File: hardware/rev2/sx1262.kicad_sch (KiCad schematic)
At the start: 35 parts, among them U2 SX1262IMLTRT, U3 PE4259, Y2 TCXO 32MHz

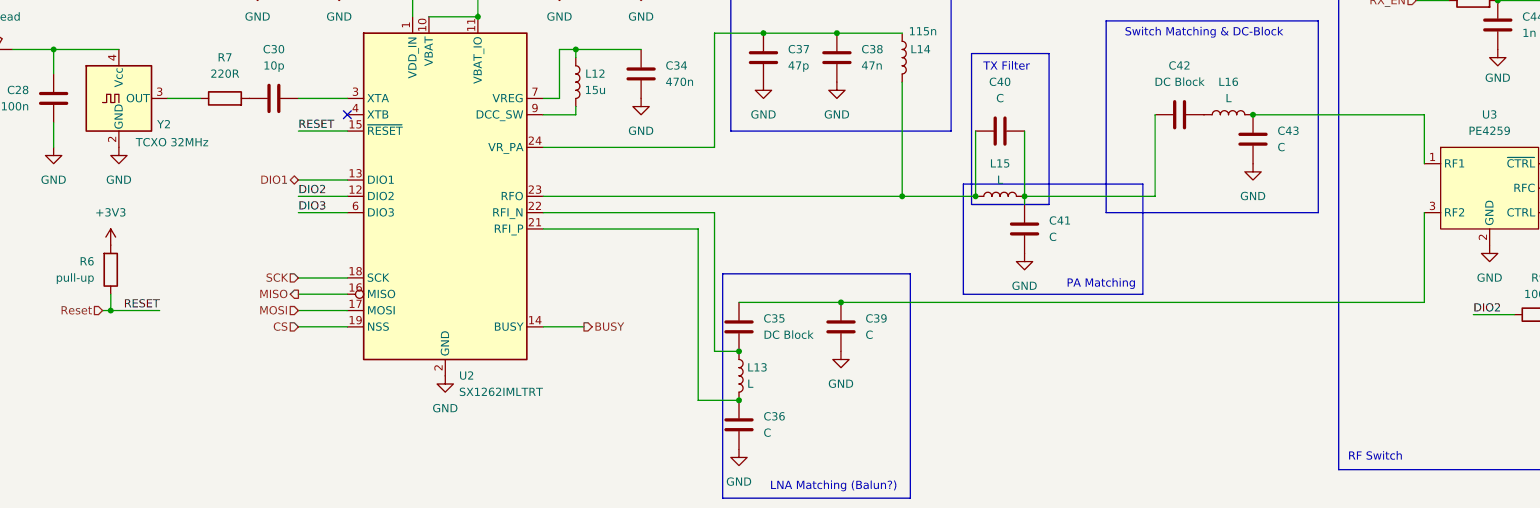
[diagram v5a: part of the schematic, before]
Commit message: fixed some ERC errors and warnings, added USB, assigned a bunch of footprints
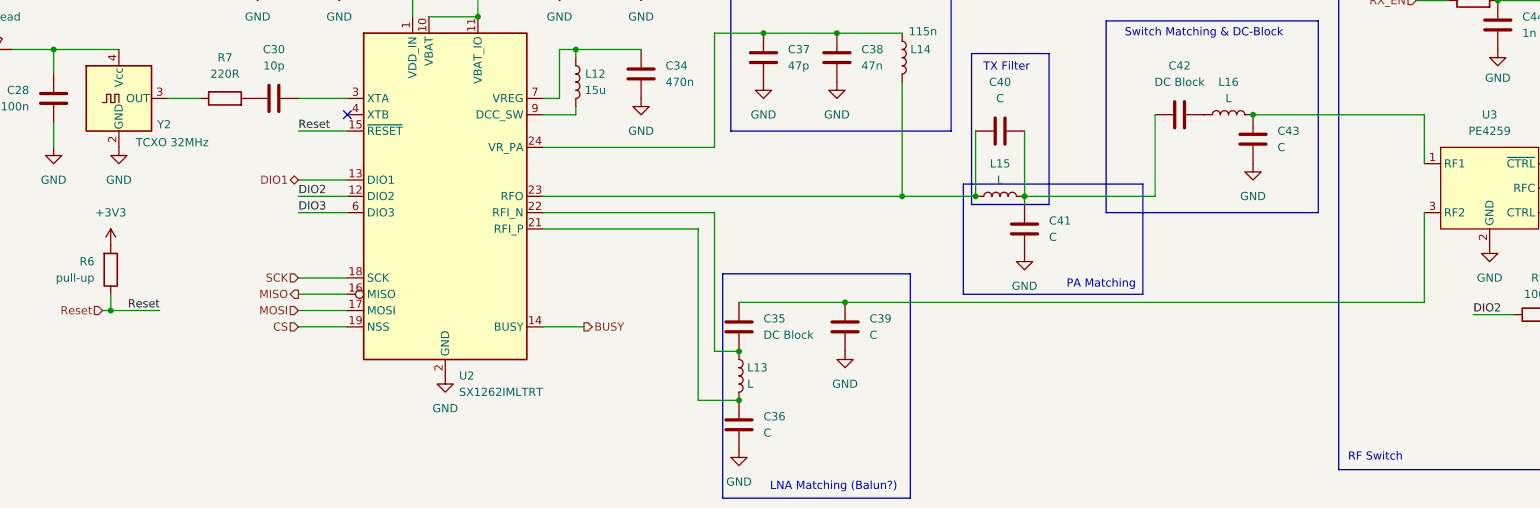
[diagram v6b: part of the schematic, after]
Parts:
- C28, C29, C30, C31, C32, C33, C34: footprint (none) -> Capacitor_SMD:C_0603_1608Metric_Pad1.08x0.95mm_HandSolder
- C35, C36, C37, C38, C39, C40, C41, C42, C43, C44, C45, C46, C47, C48: footprint (none) -> Capacitor_SMD:C_0402_1005Metric_Pad0.74x0.62mm_HandSolder
- L12, R6, R7, R8, R9: footprint (none) -> Inductor_SMD:L_0603_1608Metric_Pad1.05x0.95mm_HandSolder
- L13, L14, L15, L16, L17: footprint (none) -> Inductor_SMD:L_0402_1005Metric_Pad0.77x0.64mm_HandSolder
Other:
- moved on the sheet: C39
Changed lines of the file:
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@@
 	)
 	(junction
-		(at 284.48 106.68)
+		(at 182.88 153.67)
 		(diameter 0)
 		(color 0 0 0 0)
 	)
 	(junction
-		(at 182.245 153.67)
+		(at 284.48 106.68)
 		(diameter 0)
 		(color 0 0 0 0)
@@
 	(wire
 		(pts
-			(xy 166.37 153.67) (xy 182.245 153.67)
+			(xy 166.37 153.67) (xy 182.88 153.67)
 		)
 		(stroke
@@
 	(wire
 		(pts
-			(xy 182.245 153.67) (xy 273.05 153.67)
-		)
-		(stroke
-			(width 0)
-			(type default)
-		)
-	)
-	(wire
-		(pts
 			(xy 135.89 129.54) (xy 162.56 129.54)
 		)
@@
 	(wire
 		(pts
+			(xy 182.88 153.67) (xy 273.05 153.67)
+		)
+		(stroke
+			(width 0)
+			(type default)
+		)
+	)
+	(wire
+		(pts
 			(xy 210.82 138.43) (xy 210.82 137.16)
 		)
@@
 		)
 	)
-	(label "RESET"
+	(label "Reset"
 		(at 97.79 127 0)
 		(effects
@@
 		)
 	)
-	(label "RESET"
+	(label "Reset"
 		(at 76.2 154.94 180)
 		(effects
@@
 		(length 1.27)
 		(shape round)
-		(at 231.14 137.16 270)
+		(at 231.14 124.46 0)
 		(fields_autoplaced yes)
 		(effects
@@
 				(size 1.27 1.27)
 			)
-			(justify right bottom)
+			(justify left bottom)
 		)
 		(property "Net Class" "50 Ohm"
-			(at 232.41 136.4615 90)
+			(at 231.8385 123.19 0)
 			(hide yes)
 			(show_name no)
@@
 		)
 		(property "Component Class" ""
-			(at 62.23 -25.4 0)
+			(at 62.23 -38.1 0)
 			(show_name no)
 			(do_not_autoplace no)
@@
 			)
 		)
-		(property "Footprint" ""
+		(property "Footprint" "Capacitor_SMD:C_0603_1608Metric_Pad1.08x0.95mm_HandSolder"
 			(at 103.1748 104.14 0)
 			(hide yes)
@@
 			)
 		)
-		(property "Footprint" ""
+		(property "Footprint" "Inductor_SMD:L_0603_1608Metric_Pad1.05x0.95mm_HandSolder"
 			(at 280.67 108.458 90)
 			(hide yes)
@@
 			)
 		)
-		(property "Footprint" ""
+		(property "Footprint" "Inductor_SMD:L_0603_1608Metric_Pad1.05x0.95mm_HandSolder"
 			(at 140.97 119.38 0)
 			(hide yes)
@@
 			)
 		)
-		(property "Footprint" ""
+		(property "Footprint" "Capacitor_SMD:C_0603_1608Metric_Pad1.08x0.95mm_HandSolder"
 			(at 60.6552 118.11 0)
 			(hide yes)
@@
 			)
 		)
-		(property "Footprint" ""
+		(property "Footprint" "Capacitor_SMD:C_0402_1005Metric_Pad0.74x0.62mm_HandSolder"
 			(at 352.7552 146.05 0)
 			(hide yes)
@@
 			)
 		)
-		(property "Footprint" ""
+		(property "Footprint" "Capacitor_SMD:C_0603_1608Metric_Pad1.08x0.95mm_HandSolder"
 			(at 139.3952 104.14 0)
 			(hide yes)
@@
 			)
 		)
-		(property "Footprint" ""
+		(property "Footprint" "Capacitor_SMD:C_0402_1005Metric_Pad0.74x0.62mm_HandSolder"
 			(at 167.3352 176.53 0)
 			(hide yes)
@@
 			)
 		)
-		(property "Footprint" ""
+		(property "Footprint" "Inductor_SMD:L_0402_1005Metric_Pad0.77x0.64mm_HandSolder"
 			(at 166.37 165.1 0)
 			(hide yes)
@@
 			)
 		)
-		(property "Footprint" ""
+		(property "Footprint" "Inductor_SMD:L_0603_1608Metric_Pad1.05x0.95mm_HandSolder"
 			(at 290.83 157.353 90)
 			(hide yes)
@@
 			)
 		)
-		(property "Footprint" ""
+		(property "Footprint" "Inductor_SMD:L_0402_1005Metric_Pad0.77x0.64mm_HandSolder"
 			(at 242.57 124.46 0)
 			(hide yes)
@@
 			)
 		)
-		(property "Footprint" ""
+		(property "Footprint" "Capacitor_SMD:C_0402_1005Metric_Pad0.74x0.62mm_HandSolder"
 			(at 245.4148 124.46 0)
 			(hide yes)
@@
 	(symbol
 		(lib_id "Device:C")
-		(at 182.245 157.48 0)
+		(at 182.88 157.48 0)
 		(unit 1)
 		(body_style 1)
@@
 		(fields_autoplaced yes)
 		(property "Reference" "C39"
-			(at 186.055 156.2099 0)
+			(at 186.69 156.2099 0)
 			(show_name no)
 			(do_not_autoplace no)
@@
 		)
 		(property "Value" "C"
-			(at 186.055 158.7499 0)
+			(at 186.69 158.7499 0)
 			(show_name no)
 			(do_not_autoplace no)
@@
 			)
 		)
-		(property "Footprint" ""
-			(at 183.2102 161.29 0)
+		(property "Footprint" "Capacitor_SMD:C_0402_1005Metric_Pad0.74x0.62mm_HandSolder"
+			(at 183.8452 161.29 0)
 			(hide yes)
 			(show_name no)
@@
 		)
 		(property "Datasheet" ""
-			(at 182.245 157.48 0)
+			(at 182.88 157.48 0)
 			(hide yes)
 			(show_name no)
@@
 		)
 		(property "Description" "Unpolarized capacitor"
-			(at 182.245 157.48 0)
+			(at 182.88 157.48 0)
 			(hide yes)
 			(show_name no)
@@
 		)
 		(property "Digikey Part Number" ""
-			(at 182.245 157.48 0)
+			(at 182.88 157.48 0)
 			(hide yes)
 			(show_name no)
@@
 		)
 		(property "Mouser Part Number" ""
-			(at 182.245 157.48 0)
+			(at 182.88 157.48 0)
 			(hide yes)
 			(show_name no)
@@
 			)
 		)
-		(property "Footprint" ""
+		(property "Footprint" "Capacitor_SMD:C_0402_1005Metric_Pad0.74x0.62mm_HandSolder"
 			(at 340.0552 146.05 0)
 			(hide yes)
@@
 			)
 		)
-		(property "Footprint" ""
+		(property "Footprint" "Inductor_SMD:L_0603_1608Metric_Pad1.05x0.95mm_HandSolder"
 			(at 86.36 123.698 90)
 			(hide yes)
@@
 			)
 		)
-		(property "Footprint" ""
+		(property "Footprint" "Inductor_SMD:L_0402_1005Metric_Pad0.77x0.64mm_HandSolder"
 			(at 345.44 135.89 0)
 			(hide yes)
@@
 			)
 		)
-		(property "Footprint" ""
+		(property "Footprint" "Inductor_SMD:L_0603_1608Metric_Pad1.05x0.95mm_HandSolder"
 			(at 66.802 148.59 90)
 			(hide yes)
@@
 			)
 		)
-		(property "Footprint" ""
+		(property "Footprint" "Inductor_SMD:L_0402_1005Metric_Pad0.77x0.64mm_HandSolder"
 			(at 191.77 115.57 0)
 			(hide yes)
@@
 			)
 		)
-		(property "Footprint" ""
+		(property "Footprint" "Capacitor_SMD:C_0402_1005Metric_Pad0.74x0.62mm_HandSolder"
 			(at 171.1452 119.38 0)
 			(hide yes)
@@
 			)
 		)
-		(property "Footprint" ""
+		(property "Footprint" "Capacitor_SMD:C_0402_1005Metric_Pad0.74x0.62mm_HandSolder"
 			(at 182.5752 119.38 0)
 			(hide yes)
@@
 	(symbol
 		(lib_id "power:GND")
-		(at 182.245 161.29 0)
+		(at 182.88 161.29 0)
 		(unit 1)
 		(body_style 1)
@@
 		(fields_autoplaced yes)
 		(property "Reference" "#PWR051"
-			(at 182.245 167.64 0)
+			(at 182.88 167.64 0)
 			(hide yes)
 			(show_name no)
@@
 		)
 		(property "Value" "GND"
-			(at 182.245 166.37 0)
+			(at 182.88 166.37 0)
 			(show_name no)
 			(do_not_autoplace no)
@@
 		)
 		(property "Footprint" ""
-			(at 182.245 161.29 0)
+			(at 182.88 161.29 0)
 			(hide yes)
 			(show_name no)
@@
 		)
 		(property "Datasheet" ""
-			(at 182.245 161.29 0)
+			(at 182.88 161.29 0)
 			(hide yes)
 			(show_name no)
@@
 		)
 		(property "Description" "Power symbol creates a global label with name \"GND\" , ground"
-			(at 182.245 161.29 0)
+			(at 182.88 161.29 0)
 			(hide yes)
 			(show_name no)
@@
 			)
 		)
-		(property "Footprint" ""
+		(property "Footprint" "Inductor_SMD:L_0402_1005Metric_Pad0.77x0.64mm_HandSolder"
 			(at 207.01 137.16 0)
 			(hide yes)
@@
 			)
 		)
-		(property "Footprint" ""
+		(property "Footprint" "Capacitor_SMD:C_0603_1608Metric_Pad1.08x0.95mm_HandSolder"
 			(at 90.4748 104.14 0)
 			(hide yes)
@@
 			)
 		)
-		(property "Footprint" ""
+		(property "Footprint" "Capacitor_SMD:C_0402_1005Metric_Pad0.74x0.62mm_HandSolder"
 			(at 295.6052 163.195 0)
 			(hide yes)
@@
 			)
 		)
-		(property "Footprint" ""
+		(property "Footprint" "Capacitor_SMD:C_0402_1005Metric_Pad0.74x0.62mm_HandSolder"
 			(at 336.55 134.9248 0)
 			(hide yes)
@@
 			)
 		)
-		(property "Footprint" ""
+		(property "Footprint" "Capacitor_SMD:C_0402_1005Metric_Pad0.74x0.62mm_HandSolder"
 			(at 285.4452 114.3 0)
 			(hide yes)
@@
 			)
 		)
-		(property "Footprint" ""
+		(property "Footprint" "Capacitor_SMD:C_0402_1005Metric_Pad0.74x0.62mm_HandSolder"
 			(at 238.76 123.4948 0)
 			(hide yes)
@@
 			)
 		)
-		(property "Footprint" ""
+		(property "Footprint" "Capacitor_SMD:C_0603_1608Metric_Pad1.08x0.95mm_HandSolder"
 			(at 152.0952 104.14 0)
 			(hide yes)
@@
 			)
 		)
-		(property "Footprint" ""
+		(property "Footprint" "Capacitor_SMD:C_0603_1608Metric_Pad1.08x0.95mm_HandSolder"
 			(at 97.79 120.9548 0)
 			(hide yes)
@@
 			)
 		)
-		(property "Footprint" ""
+		(property "Footprint" "Capacitor_SMD:C_0402_1005Metric_Pad0.74x0.62mm_HandSolder"
 			(at 210.82 126.0348 0)
 			(hide yes)
@@
 			)
 		)
-		(property "Footprint" ""
+		(property "Footprint" "Capacitor_SMD:C_0603_1608Metric_Pad1.08x0.95mm_HandSolder"
 			(at 152.0952 121.92 0)
 			(hide yes)
@@
 			)
 		)
-		(property "Footprint" ""
+		(property "Footprint" "Capacitor_SMD:C_0402_1005Metric_Pad0.74x0.62mm_HandSolder"
 			(at 211.7852 146.05 0)
 			(hide yes)
@@
 			)
 		)
-		(property "Footprint" ""
+		(property "Footprint" "Capacitor_SMD:C_0402_1005Metric_Pad0.74x0.62mm_HandSolder"
 			(at 167.3352 161.29 0)
 			(hide yes)

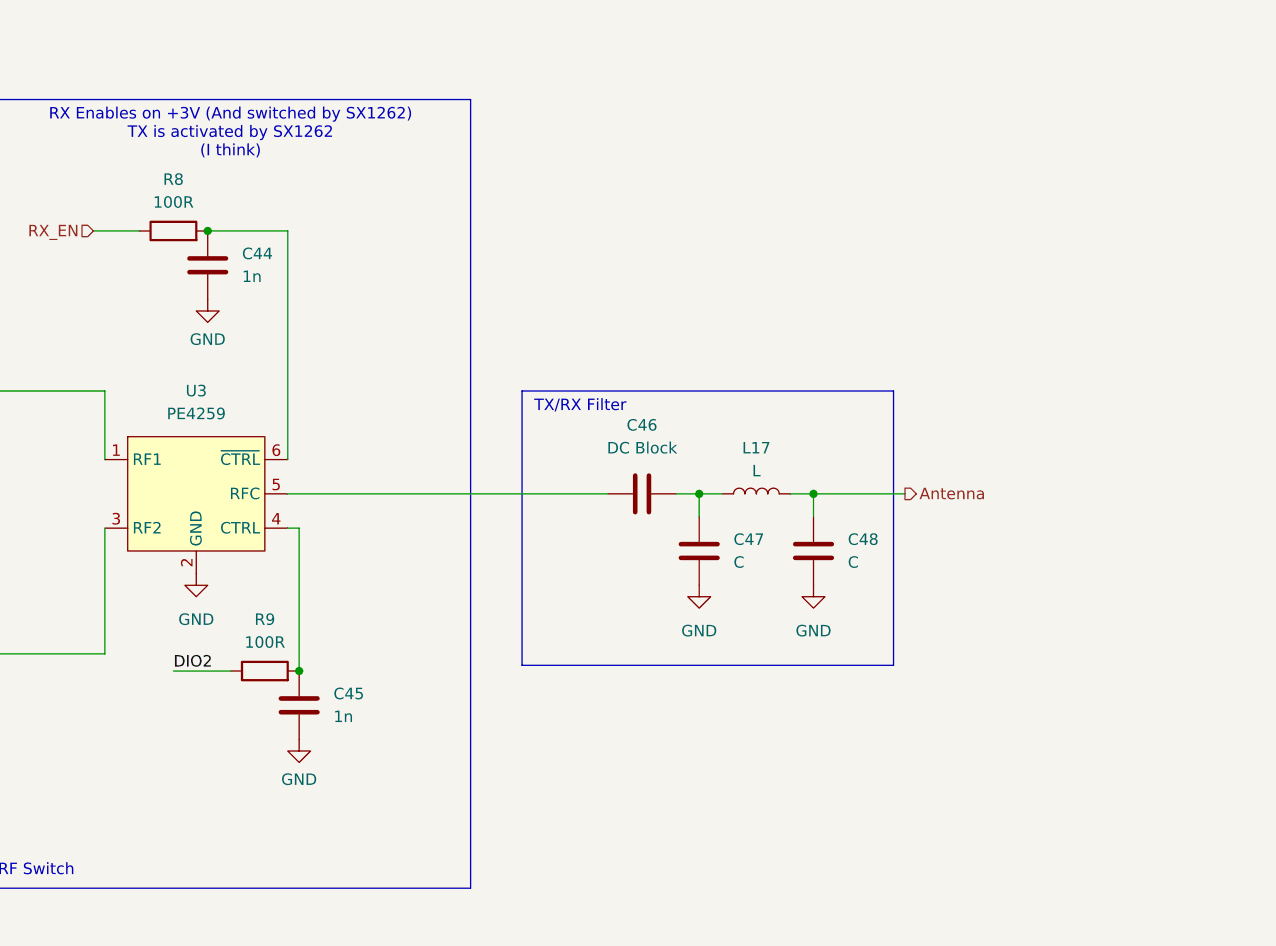
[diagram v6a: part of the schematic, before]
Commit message: ESP32 approaching final schematic. tidied up a lot and changed GPIO pins.
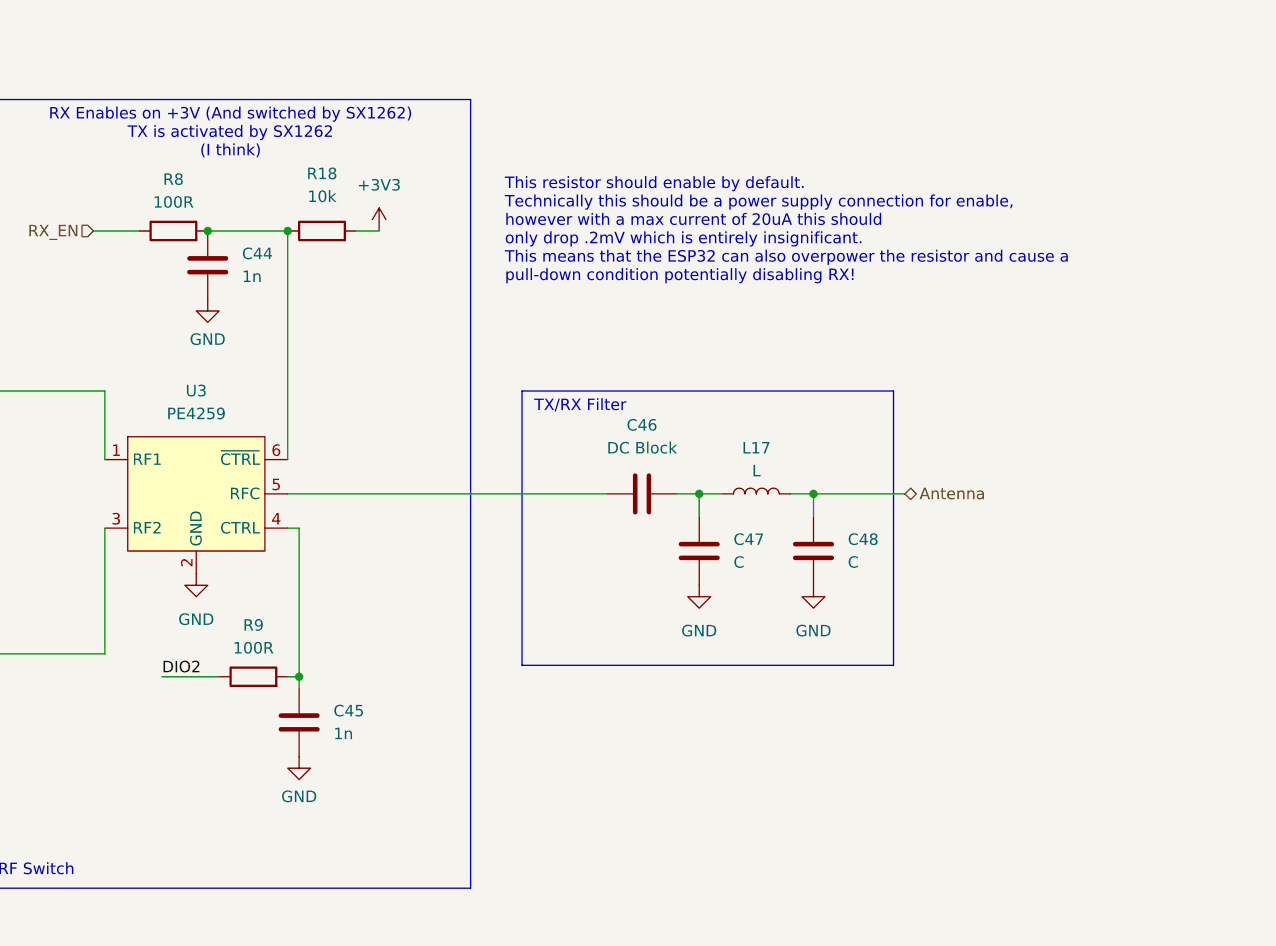
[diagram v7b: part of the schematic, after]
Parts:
- added R18: 10k, Inductor_SMD:L_0603_1608Metric_Pad1.05x0.95mm_HandSolder, symbol Device:R
- U3: footprint Package_TO_SOT_SMD:SOT-363_SC-70-6_Handsoldering -> Package_TO_SOT_SMD:SOT-363_SC-70-6
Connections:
- net +3V3: now also R18.2
- net at C44.1, R8.2, U3.6 (~{CTRL}): now also R18.1
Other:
- note added: "This resistor should enable by default. Technically this should be a power supply connection for enable, however with a max current of 20uA this should only drop .2mV which is entirely insignificant. This means that the ESP32 can also overpower the resistor and cause a pull-down condition potentially disabling RX!"
- company: (none) -> MMCX11
- moved on the sheet: C45, R9
